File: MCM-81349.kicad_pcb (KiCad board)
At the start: 2 copper layers, 65 x 65 mm, 166 parts, among them J1 Conn_01x04, J10 JACK-L-LKWGPC-5A(R), J11 Conn_02x02_Odd_Even, J2 /, J5 USB4105-GF-A, J7 Conn_01x04, J9 /, Q1 BUK9K61-100LX, Q2 BUK9K61-100LX, Q3 BUK9K61-100LX, Q8 BC846BLT1G, U1 AZ1117CR-3.3TRG1, U2 LMR16006YDDCR, U3 TMUX1219DCKR, U4 MLX81349-KLW-AMX-000, U5 ESP32-S3-WROOM-1-N16R8, U6 TXS0102DCTT, U7 BTH50060-1LUA, U8 BUK7Y38-100E

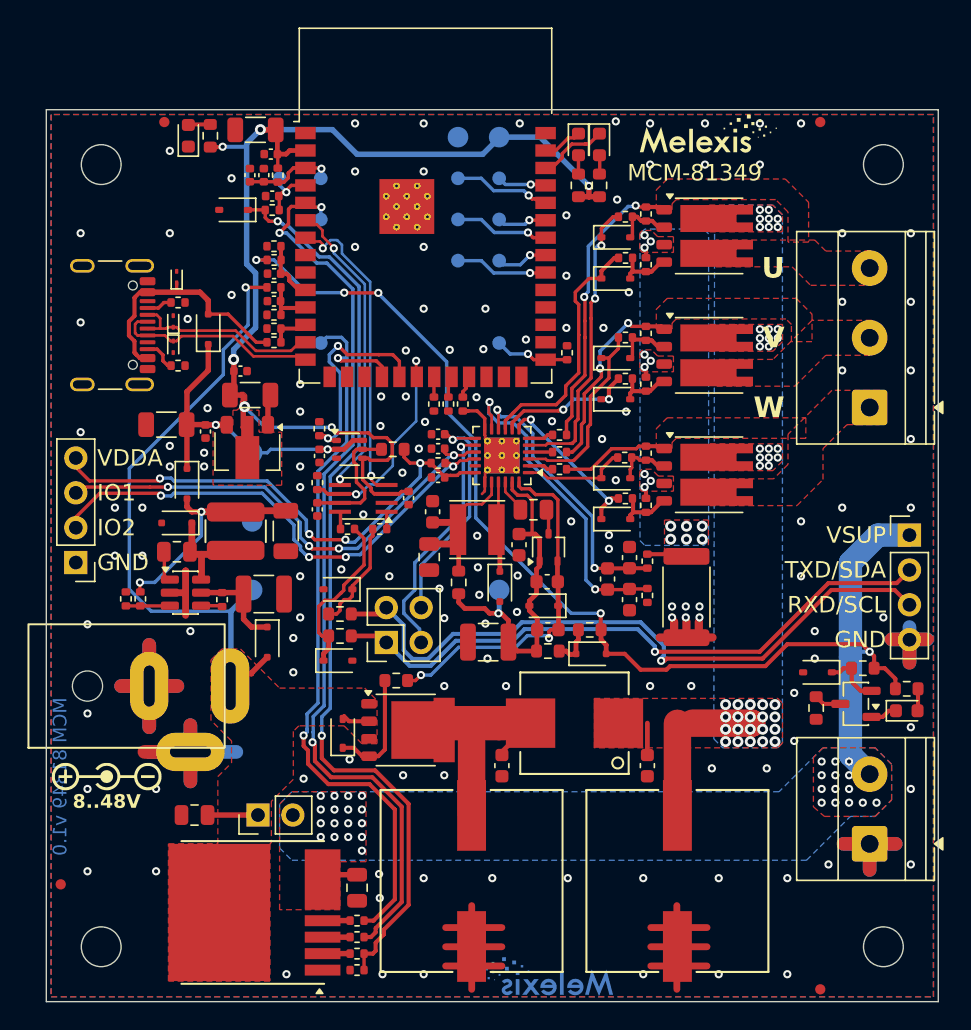
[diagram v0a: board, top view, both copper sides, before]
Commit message: improve high current tracks
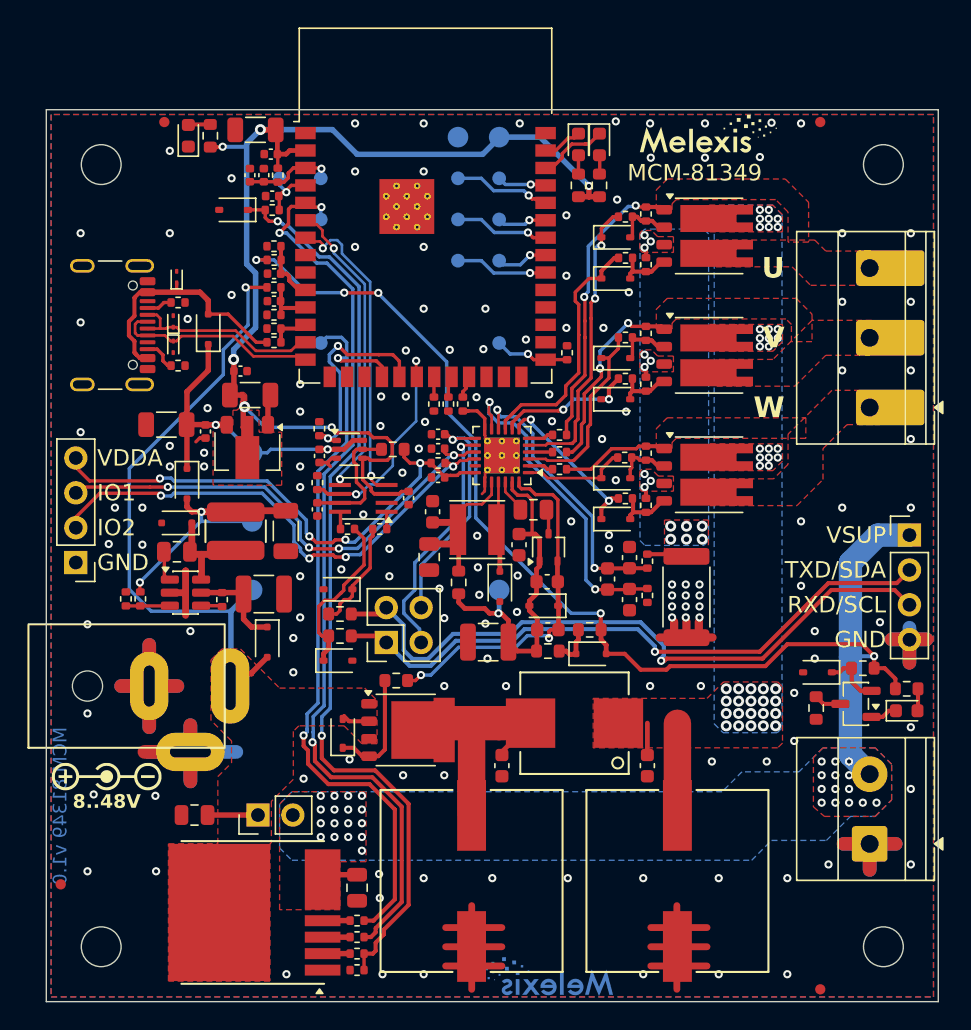
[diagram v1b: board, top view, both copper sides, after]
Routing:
- net VMOTOR: track 14.8 -> 9.05 mm
- net GND: track 13.6 -> 16.1 mm, vias 137 -> 143

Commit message: add weee and esd logo, generate fabrication info
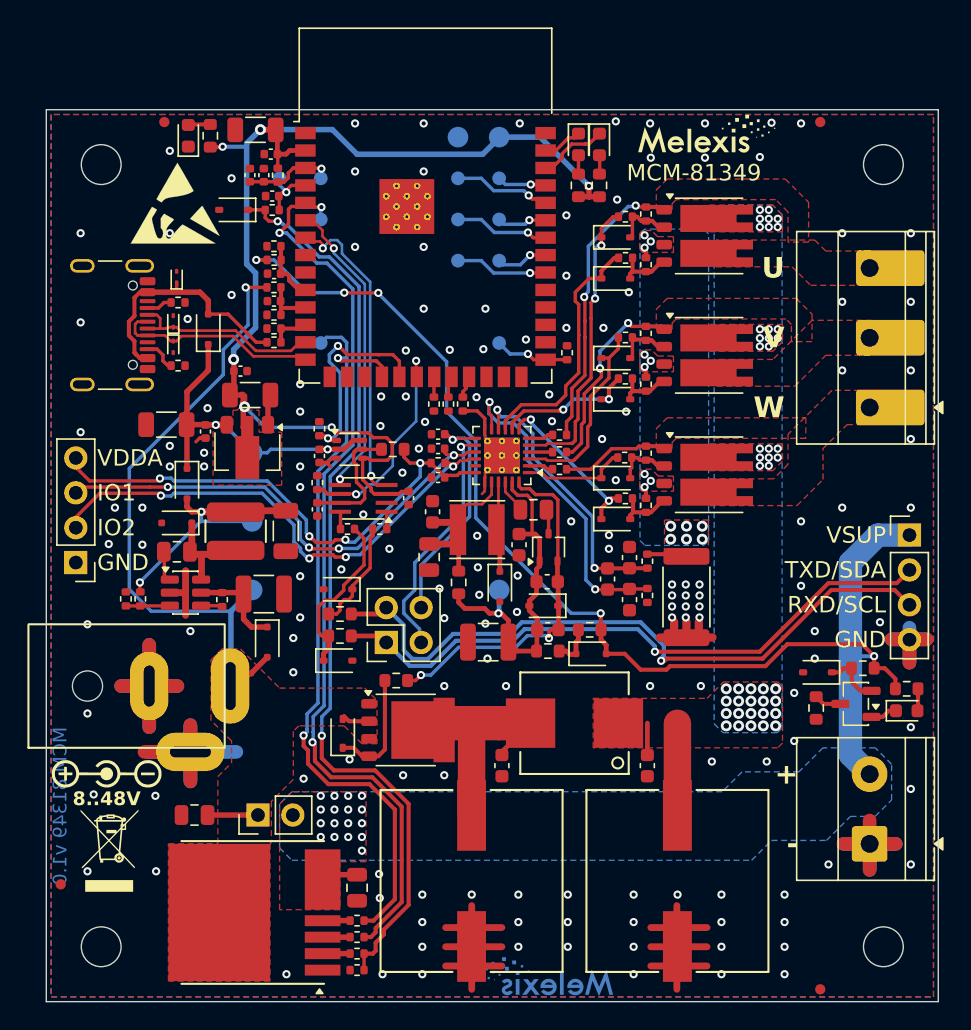
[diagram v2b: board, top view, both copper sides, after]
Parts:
- added REF**: WEEE-Logo_4.2x6mm_SilkScreen, Symbol:WEEE-Logo_4.2x6mm_SilkScreen, F.Cu at (64.6, 99.0)
- added REF**: ESD-Logo_6.6x6mm_SilkScreen, Symbol:ESD-Logo_6.6x6mm_SilkScreen, F.Cu at (69.4, 51.8)
- moved G*** 0.20 mm to (64.4, 93.4)
- moved LOG1 0.12 mm to (103.1, 48.1)
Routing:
- net VBUS: vias 36 -> 22
- net GND: vias 143 -> 157
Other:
- board text added: "+"
- board text added: "-"
